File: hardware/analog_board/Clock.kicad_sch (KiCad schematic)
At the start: 12 parts, among them J3 Conn_01x04_Pin, U8 CDCI6214RGER, Y1 ASE-10MHz

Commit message: feat：模拟板电源 原理图设计
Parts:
- J3: footprint (none) -> Connector_PinHeader_2.54mm:PinHeader_1x04_P2.54mm_Vertical
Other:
- moved on the sheet: Y1
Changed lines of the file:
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@@
 	)
 	(no_connect
-		(at 40.64 58.42)
+		(at 40.64 57.15)
 	)
 	(no_connect
@@
 	(wire
 		(pts
-			(xy 48.26 48.26) (xy 48.26 50.8)
+			(xy 48.26 46.99) (xy 48.26 49.53)
 		)
 		(stroke
@@
 	(wire
 		(pts
-			(xy 48.26 68.58) (xy 48.26 66.04)
+			(xy 48.26 67.31) (xy 48.26 64.77)
 		)
 		(stroke
@@
 	(wire
 		(pts
-			(xy 55.88 58.42) (xy 64.77 58.42)
+			(xy 55.88 57.15) (xy 64.77 57.15)
 		)
 		(stroke
@@
 	)
 	(label "CLK_{IN}"
-		(at 58.42 58.42 0)
+		(at 58.42 57.15 0)
 		(effects
 			(font
@@
 		)
 		(property "Value" "Clock_V_{DD}"
-			(at 127.0001 154.94 90)
+			(at 129.54 157.4799 0)
 			(show_name no)
 			(do_not_autoplace no)
@@
 			)
 		)
-		(property "Footprint" ""
+		(property "Footprint" "Connector_PinHeader_2.54mm:PinHeader_1x04_P2.54mm_Vertical"
 			(at 99.06 55.88 0)
 			(hide yes)
@@
 		)
 		(property "Value" "GND"
-			(at 142.24 133.35 0)
-			(show_name no)
-			(do_not_autoplace no)
-			(effects
-				(font
-					(size 1.27 1.27)
-				)
+			(at 144.78 129.5399 0)
+			(show_name no)
+			(do_not_autoplace no)
+			(effects
+				(font
+					(size 1.27 1.27)
+				)
+				(justify left)
 			)
 		)
@@
 		)
 		(property "Value" "GND"
-			(at 106.68 68.58 0)
-			(show_name no)
-			(do_not_autoplace no)
-			(effects
-				(font
-					(size 1.27 1.27)
-				)
+			(at 109.22 64.7699 0)
+			(show_name no)
+			(do_not_autoplace no)
+			(effects
+				(font
+					(size 1.27 1.27)
+				)
+				(justify left)
 			)
 		)
@@
 	(symbol
 		(lib_id "power:+1V8")
-		(at 48.26 48.26 0)
+		(at 48.26 46.99 0)
 		(unit 1)
 		(body_style 1)
@@
 		(fields_autoplaced yes)
 		(property "Reference" "#PWR0122"
-			(at 48.26 52.07 0)
+			(at 48.26 50.8 0)
 			(hide yes)
 			(show_name no)
@@
 		)
 		(property "Value" "Clock_V_{TCXO}"
-			(at 48.26 43.18 0)
-			(show_name no)
-			(do_not_autoplace no)
-			(effects
-				(font
-					(size 1.27 1.27)
-				)
+			(at 50.8 45.7199 0)
+			(show_name no)
+			(do_not_autoplace no)
+			(effects
+				(font
+					(size 1.27 1.27)
+				)
+				(justify left)
 			)
 		)
 		(property "Footprint" ""
-			(at 48.26 48.26 0)
+			(at 48.26 46.99 0)
 			(hide yes)
 			(show_name no)
@@
 		)
 		(property "Datasheet" ""
-			(at 48.26 48.26 0)
+			(at 48.26 46.99 0)
 			(hide yes)
 			(show_name no)
@@
 		)
 		(property "Description" "Power symbol creates a global label with name \"+1V8\""
-			(at 48.26 48.26 0)
+			(at 48.26 46.99 0)
 			(hide yes)
 			(show_name no)
@@
 	(symbol
 		(lib_id "Oscillator:ASE-xxxMHz")
-		(at 48.26 58.42 0)
+		(at 48.26 57.15 0)
 		(unit 1)
 		(body_style 1)
@@
 		(dnp no)
 		(property "Reference" "Y1"
-			(at 39.37 48.768 0)
+			(at 39.37 47.498 0)
 			(show_name no)
 			(do_not_autoplace no)
@@
 		)
 		(property "Value" "ASE-10MHz"
-			(at 39.37 51.308 0)
+			(at 39.37 50.038 0)
 			(show_name no)
 			(do_not_autoplace no)
@@
 		)
 		(property "Footprint" "Oscillator:Oscillator_SMD_Abracon_ASE-4Pin_3.2x2.5mm"
-			(at 66.04 67.31 0)
+			(at 66.04 66.04 0)
 			(hide yes)
 			(show_name no)
@@
 		)
 		(property "Datasheet" "http://www.abracon.com/Oscillators/ASV.pdf"
-			(at 45.72 58.42 0)
+			(at 45.72 57.15 0)
 			(hide yes)
 			(show_name no)
@@
 		)
 		(property "Description" "3.3V CMOS SMD Crystal Clock Oscillator, Abracon"
-			(at 48.26 58.42 0)
+			(at 48.26 57.15 0)
 			(hide yes)
 			(show_name no)
@@
 		)
 		(property "Value" "Clock_V_{DD}"
-			(at 76.2 153.67 0)
-			(show_name no)
-			(do_not_autoplace no)
-			(effects
-				(font
-					(size 1.27 1.27)
-				)
+			(at 78.74 157.4799 0)
+			(show_name no)
+			(do_not_autoplace no)
+			(effects
+				(font
+					(size 1.27 1.27)
+				)
+				(justify left)
 			)
 		)
@@
 		)
 		(property "Value" "GND"
-			(at 127 187.96 0)
-			(show_name no)
-			(do_not_autoplace no)
-			(effects
-				(font
-					(size 1.27 1.27)
-				)
+			(at 129.54 184.1499 0)
+			(show_name no)
+			(do_not_autoplace no)
+			(effects
+				(font
+					(size 1.27 1.27)
+				)
+				(justify left)
 			)
 		)
@@
 	(symbol
 		(lib_id "power:GND")
-		(at 48.26 68.58 0)
+		(at 48.26 67.31 0)
 		(unit 1)
 		(body_style 1)
@@
 		(fields_autoplaced yes)
 		(property "Reference" "#PWR083"
-			(at 48.26 74.93 0)
+			(at 48.26 73.66 0)
 			(hide yes)
 			(show_name no)
@@
 		)
 		(property "Value" "GND"
-			(at 48.26 73.66 0)
-			(show_name no)
-			(do_not_autoplace no)
-			(effects
-				(font
-					(size 1.27 1.27)
-				)
+			(at 50.8 68.5799 0)
+			(show_name no)
+			(do_not_autoplace no)
+			(effects
+				(font
+					(size 1.27 1.27)
+				)
+				(justify left)
 			)
 		)
 		(property "Footprint" ""
-			(at 48.26 68.58 0)
+			(at 48.26 67.31 0)
 			(hide yes)
 			(show_name no)
@@
 		)
 		(property "Datasheet" ""
-			(at 48.26 68.58 0)
+			(at 48.26 67.31 0)
 			(hide yes)
 			(show_name no)
@@
 		)
 		(property "Description" "Power symbol creates a global label with name \"GND\" , ground"
-			(at 48.26 68.58 0)
+			(at 48.26 67.31 0)
 			(hide yes)
 			(show_name no)
@@
 		)
 		(property "Value" "GND"
-			(at 171.4499 77.47 90)
+			(at 173.99 80.0099 0)
 			(show_name no)
 			(do_not_autoplace no)
@@
 		)
 		(property "Value" "Clock_V_{DD}"
-			(at 105.41 95.2499 90)
-			(show_name no)
-			(do_not_autoplace no)
-			(effects
-				(font
-					(size 1.27 1.27)
-				)
-				(justify left)
+			(at 107.95 92.71 90)
+			(show_name no)
+			(do_not_autoplace no)
+			(effects
+				(font
+					(size 1.27 1.27)
+				)
 			)
 		)
@@
 		)
 		(property "Value" "Clock_V_{VCO}"
-			(at 165.1 82.55 0)
-			(show_name no)
-			(do_not_autoplace no)
-			(effects
-				(font
-					(size 1.27 1.27)
-				)
+			(at 167.64 86.3599 0)
+			(show_name no)
+			(do_not_autoplace no)
+			(effects
+				(font
+					(size 1.27 1.27)
+				)
+				(justify left)
 			)
 		)
@@
 		)
 		(property "Value" "GND"
-			(at 76.2 185.42 0)
-			(show_name no)
-			(do_not_autoplace no)
-			(effects
-				(font
-					(size 1.27 1.27)
-				)
-			)
-		)
+			(at 78.74 181.6099 0)
+			(show_name no)
+			(do_not_autoplace no)
+			(effects
+				(font
+					(size 1.27 1.27)
+				)
+				(justify left)
+			)
+		)

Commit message: feat：时钟电路预布局
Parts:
- R53, R54, R55, R56, R57: footprint Resistor_SMD:R_0402_1005Metric -> Capacitor_SMD:C_0603_1608Metric
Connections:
- net DAC_CKL- renamed DAC_CLK-
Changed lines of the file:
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@@
 		(at 120.65 90.17)
+	)
+	(bus_entry
+		(at 116.84 99.06)
+		(size 2.54 2.54)
+		(stroke
+			(width 0)
+			(type default)
+		)
 	)
 	(wire
@@
 		)
 	)
+	(hierarchical_label "DAC_CLK+"
+		(shape input)
+		(at 176.53 95.25 0)
+		(effects
+			(font
+				(size 1.27 1.27)
+			)
+			(justify left)
+		)
+	)
+	(hierarchical_label "DAC_CLK-"
+		(shape input)
+		(at 176.53 97.79 0)
+		(effects
+			(font
+				(size 1.27 1.27)
+			)
+			(justify left)
+		)
+	)
 	(hierarchical_label "Clock_NRST"
 		(shape input)
@@
 		(shape output)
 		(at 176.53 107.95 0)
-		(effects
-			(font
-				(size 1.27 1.27)
-			)
-			(justify left)
-		)
-	)
-	(hierarchical_label "DAC_CLK+"
-		(shape output)
-		(at 176.53 95.25 0)
-		(effects
-			(font
-				(size 1.27 1.27)
-			)
-			(justify left)
-		)
-	)
-	(hierarchical_label "DAC_CKL-"
-		(shape output)
-		(at 176.53 97.79 0)
 		(effects
 			(font
@@
 			)
 		)
-		(property "Footprint" "Resistor_SMD:R_0402_1005Metric"
+		(property "Footprint" "Capacitor_SMD:C_0603_1608Metric"
 			(at 128.778 163.83 90)
 			(hide yes)
@@
 			)
 		)
-		(property "Footprint" "Resistor_SMD:R_0402_1005Metric"
+		(property "Footprint" "Capacitor_SMD:C_0603_1608Metric"
 			(at 169.672 86.36 90)
 			(hide yes)
@@
 			)
 		)
-		(property "Footprint" "Resistor_SMD:R_0402_1005Metric"
+		(property "Footprint" "Capacitor_SMD:C_0603_1608Metric"
 			(at 118.11 56.642 90)
 			(hide yes)
@@
 			)
 		)
-		(property "Footprint" "Resistor_SMD:R_0402_1005Metric"
+		(property "Footprint" "Capacitor_SMD:C_0603_1608Metric"
 			(at 115.57 96.012 90)
 			(hide yes)
@@
 			)
 		)
-		(property "Footprint" "Resistor_SMD:R_0402_1005Metric"
+		(property "Footprint" "Capacitor_SMD:C_0603_1608Metric"
 			(at 118.11 54.102 90)
 			(hide yes)

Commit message: feat：根据PCB微调原理图
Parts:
- added J7: CH1, Connector_Coaxial:SMA_BAT_Wireless_BWSMA-KWE-Z001, symbol Connector:Conn_Coaxial_Small
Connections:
- net 10MHz_OUT: now also J7.1 (In)
- net GND: now also J7.2 (Ext)
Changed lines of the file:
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@@
+	(wire
+		(pts
+			(xy 199.39 53.34) (xy 199.39 55.88)
+		)
+		(stroke
+			(width 0)
+			(type default)
+		)
+	)
 	(wire
 		(pts
@@
 	(wire
 		(pts
+			(xy 196.85 53.34) (xy 199.39 53.34)
+		)
+		(stroke
+			(width 0)
+			(type default)
+		)
+	)
+	(wire
+		(pts
 			(xy 107.95 107.95) (xy 120.65 107.95)
 		)
@@
 		(pts
 			(xy 90.17 170.18) (xy 97.79 170.18)
+		)
+		(stroke
+			(width 0)
+			(type default)
+		)
+	)
+	(wire
+		(pts
+			(xy 180.34 53.34) (xy 191.77 53.34)
 		)
 		(stroke
@@
 	(label "10MHz_OUT"
 		(at 107.95 105.41 0)
+		(effects
+			(font
+				(size 1.27 1.27)
+			)
+			(justify left bottom)
+		)
+	)
+	(label "10MHz_OUT"
+		(at 180.34 53.34 0)
 		(effects
 			(font
@@
 	)
 	(hierarchical_label "DAC_CLK-"
-		(shape input)
+		(shape output)
 		(at 176.53 97.79 0)
 		(effects
@@
 	)
 	(symbol
+		(lib_id "power:GND")
+		(at 199.39 55.88 0)
+		(unit 1)
+		(body_style 1)
+		(exclude_from_sim no)
+		(in_bom yes)
+		(on_board yes)
+		(in_pos_files yes)
+		(dnp no)
+		(fields_autoplaced yes)
+		(property "Reference" "#PWR0118"
+			(at 199.39 62.23 0)
+			(hide yes)
+			(show_name no)
+			(do_not_autoplace no)
+			(effects
+				(font
+					(size 1.27 1.27)
+				)
+			)
+		)
+		(property "Value" "GND"
+			(at 199.39 60.96 0)
+			(show_name no)
+			(do_not_autoplace no)
+			(effects
+				(font
+					(size 1.27 1.27)
+				)
+			)
+		)
+		(property "Footprint" ""
+			(at 199.39 55.88 0)
+			(hide yes)
+			(show_name no)
+			(do_not_autoplace no)
+			(effects
+				(font
+					(size 1.27 1.27)
+				)
+			)
+		)
+		(property "Datasheet" ""
+			(at 199.39 55.88 0)
+			(hide yes)
+			(show_name no)
+			(do_not_autoplace no)
+			(effects
+				(font
+					(size 1.27 1.27)
+				)
+			)
+		)
+		(property "Description" "Power symbol creates a global label with name \"GND\" , ground"
+			(at 199.39 55.88 0)
+			(hide yes)
+			(show_name no)
+			(do_not_autoplace no)
+			(effects
+				(font
+					(size 1.27 1.27)
+				)
+			)
+		)
+		(pin "1"
+		)
+		(instances
+			(project "analog_board"
+				(path "/ca4be128-f2cd-4bef-b262-ed123f9c630d/2e7e8b08-0bd8-45f7-9050-e3d0fbfdd30b"
+					(reference "#PWR0118")
+					(unit 1)
+				)
+			)
+		)
+	)
+	(symbol
 		(lib_id "power:+1V8")
 		(at 48.26 46.99 0)
@@
 					(unit 1)
 				)
+			)
+		)
+	)
+	(symbol
+		(lib_id "Connector:Conn_Coaxial_Small")
+		(at 194.31 53.34 0)
+		(unit 1)
+		(body_style 1)
+		(exclude_from_sim no)
+		(in_bom yes)
+		(on_board yes)
+		(in_pos_files yes)
+		(dnp no)
+		(property "Reference" "J7"
+			(at 202.946 52.07 0)
+			(show_name no)
+			(do_not_autoplace no)
+			(effects
+				(font
+					(size 1.27 1.27)
+				)
+			)
+		)
+		(property "Value" "CH1"
+			(at 202.946 54.61 0)
+			(show_name no)
+			(do_not_autoplace no)
+			(effects
+				(font
+					(size 1.27 1.27)
+				)
+			)
+		)
+		(property "Footprint" "Connector_Coaxial:SMA_BAT_Wireless_BWSMA-KWE-Z001"
+			(at 194.31 53.34 0)
+			(hide yes)
+			(show_name no)
+			(do_not_autoplace no)
+			(effects
+				(font
+					(size 1.27 1.27)
+				)
+			)
+		)
+		(property "Datasheet" ""
+			(at 194.31 53.34 0)
+			(hide yes)
+			(show_name no)
+			(do_not_autoplace no)
+			(effects
+				(font
+					(size 1.27 1.27)
+				)
+			)
+		)
+		(property "Description" "small coaxial connector (BNC, SMA, SMB, SMC, Cinch/RCA, LEMO, ...)"
+			(at 194.31 53.34 0)
+			(hide yes)
+			(show_name no)
+			(do_not_autoplace no)
+			(effects
+				(font
+					(size 1.27 1.27)
+				)
+			)
+		)
+		(pin "2"
+		)
+		(pin "1"
+		)
+		(instances
+			(project "analog_board"
+				(path "/ca4be128-f2cd-4bef-b262-ed123f9c630d/2e7e8b08-0bd8-45f7-9050-e3d0fbfdd30b"
+					(reference "J7")
+					(unit 1)
+				)

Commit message: feat：添加平衡铜
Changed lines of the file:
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@@
 		(in_pos_files yes)
 		(dnp no)
-		(fields_autoplaced yes)
 		(property "Reference" "#PWR0109"
 			(at 113.03 95.25 0)
@@
 		)
 		(property "Value" "Clock_V_{DD}"
-			(at 107.95 92.71 90)
+			(at 100.584 95.25 90)
 			(show_name no)
 			(do_not_autoplace no)
@@
 		(in_pos_files yes)
 		(dnp no)
-		(fields_autoplaced yes)
 		(property "Reference" "#PWR0114"
 			(at 165.1 91.44 0)
@@
 		)
 		(property "Value" "Clock_V_{VCO}"
-			(at 167.64 86.3599 0)
+			(at 159.766 83.058 0)
 			(show_name no)
 			(do_not_autoplace no)

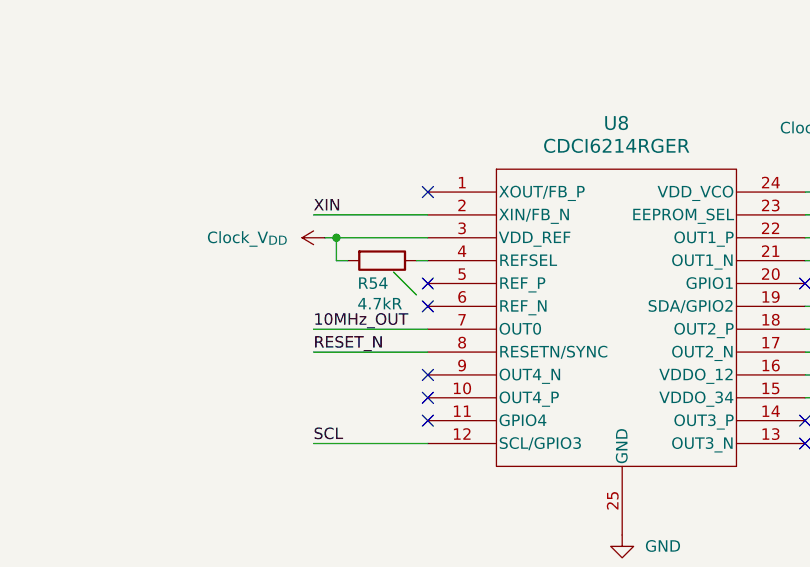
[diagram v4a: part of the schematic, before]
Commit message: feat：导出模拟板 BOM
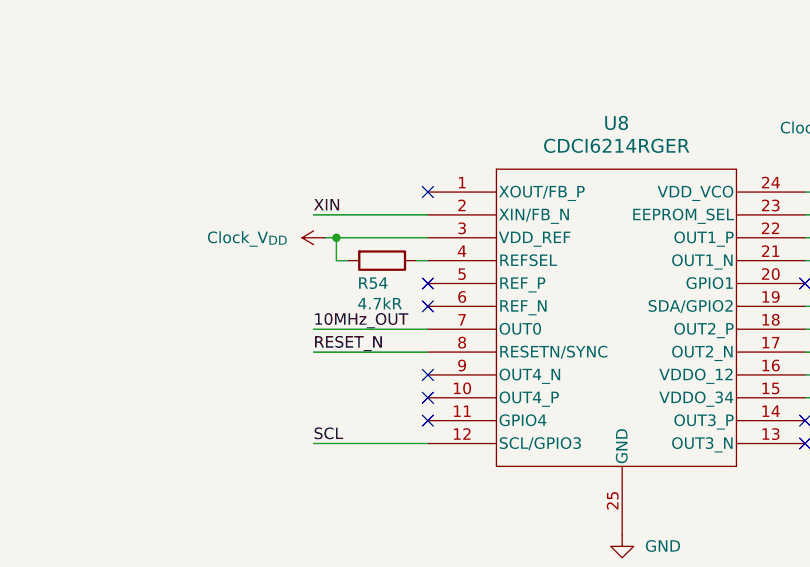
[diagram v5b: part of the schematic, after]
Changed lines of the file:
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@@
 		(at 120.65 90.17)
-	)
-	(bus_entry
-		(at 116.84 99.06)
-		(size 2.54 2.54)
-		(stroke
-			(width 0)
-			(type default)
-		)
 	)
 	(wire
@@
 			(justify left bottom)
 		)
-		(property "网络类" "LVDS_CLK"
-			(at 94.742 105.41 0)
+		(property "网络类" "50Ω"
+			(at 100.076 105.41 0)
 			(show_name no)
 			(do_not_autoplace no)
